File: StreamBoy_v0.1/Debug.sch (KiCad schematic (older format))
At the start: 7 parts

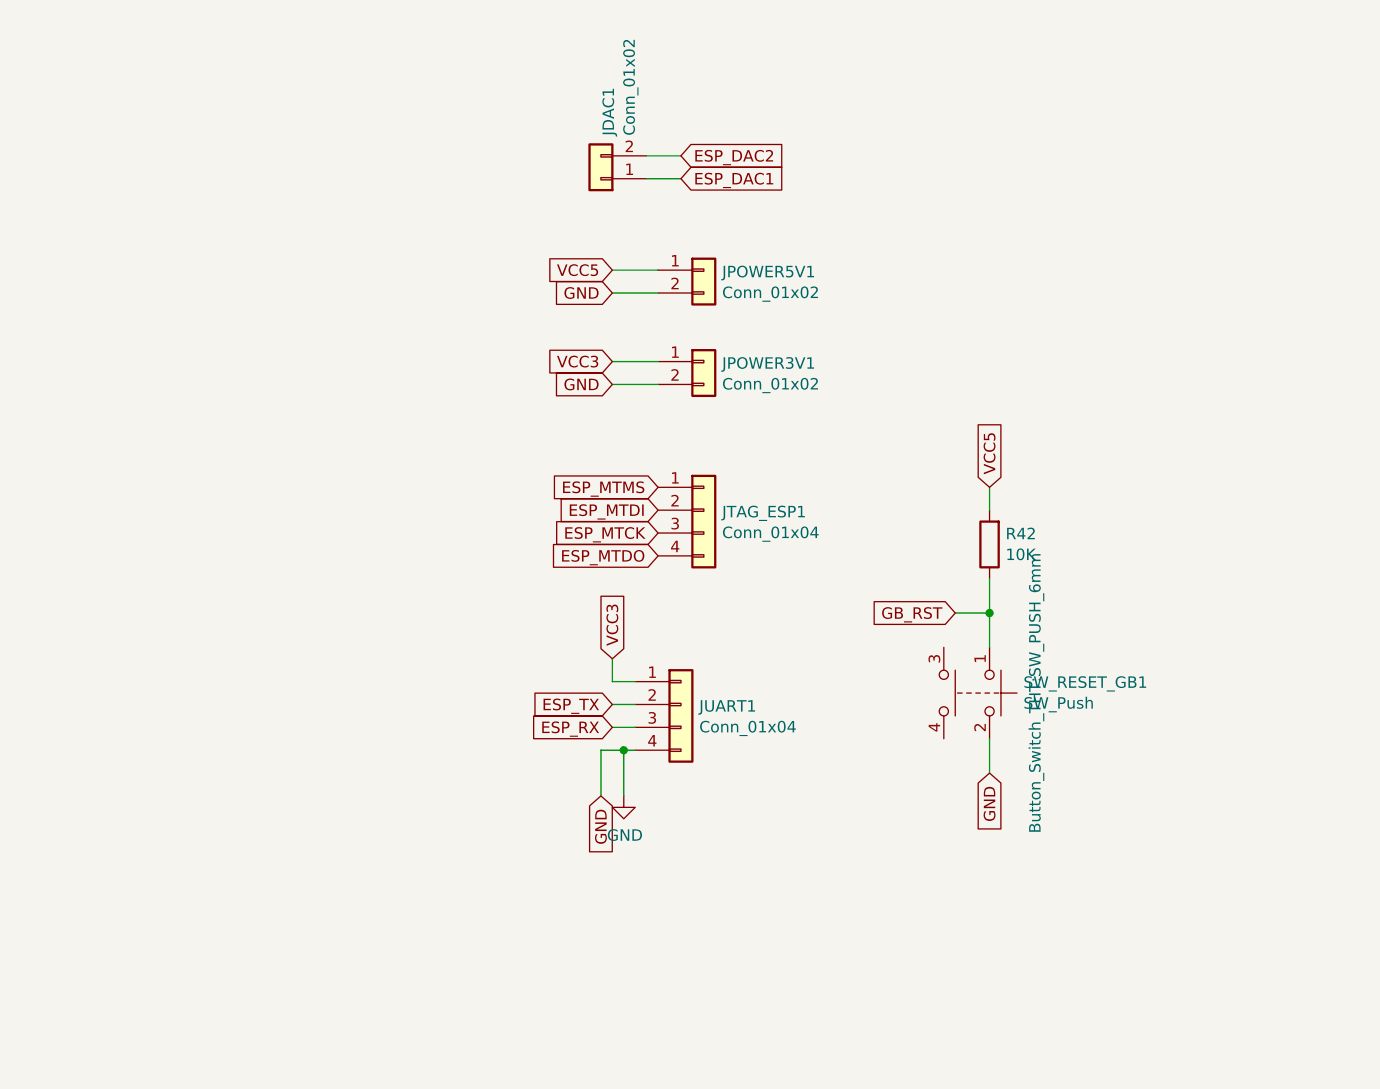
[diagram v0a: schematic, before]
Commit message: Add more debug pins
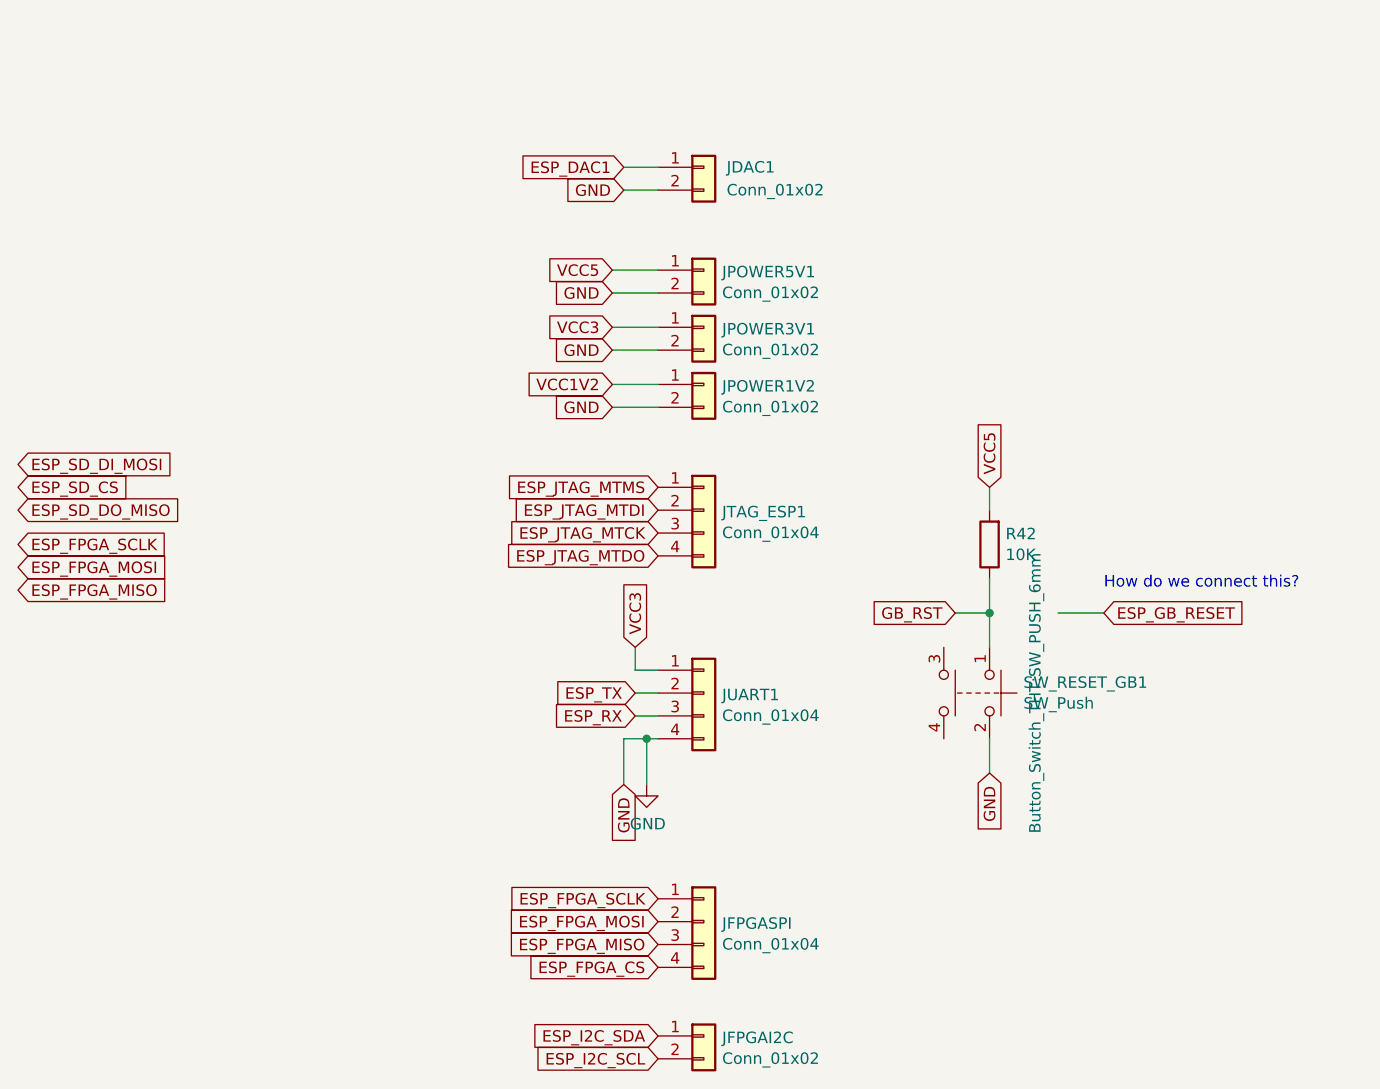
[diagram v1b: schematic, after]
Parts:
- added JFPGAI2C, JPOWER1V2: Conn_01x02, Connector_PinHeader_2.54mm:PinHeader_1x02_P2.54mm_Vertical, symbol Connector_Generic:Conn_01x02
- added JFPGASPI: Conn_01x04, Connector_PinHeader_2.54mm:PinHeader_1x04_P2.54mm_Vertical, symbol Connector_Generic:Conn_01x04
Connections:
- net labels added: ESP_FPGA_CS, ESP_FPGA_MISO, ESP_FPGA_MOSI, ESP_FPGA_SCLK, ESP_GB_RESET, ESP_I2C_SCL, ESP_I2C_SDA, ESP_JTAG_MTCK, ESP_JTAG_MTDI, ESP_JTAG_MTDO, ESP_JTAG_MTMS, ESP_SD_CS, ESP_SD_DI_MOSI, ESP_SD_DO_MISO, VCC1V2
- net labels removed: ESP_DAC2, ESP_MTCK, ESP_MTDI, ESP_MTDO, ESP_MTMS
- wire segments 19 -> 22
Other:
- note added: "How do we connect this?"
- moved on the sheet: JDAC1, JPOWER3V1, JUART1
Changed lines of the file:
@@
 EESchema Schematic File Version 4
-EELAYER 30 0
+LIBS:StreamBoy-cache
+EELAYER 29 0
 EELAYER END
 $Descr A4 11693 8268
@@
 L Connector_Generic:Conn_01x02 JPOWER3V?
 U 1 1 5E0943CE
-P 7500 2350
+P 7500 2200
 AR Path="/5E0943CE" Ref="JPOWER3V?"  Part="1"
 AR Path="/5E087685/5E0943CE" Ref="JPOWER3V1"  Part="1"
-F 0 "JPOWER3V1" H 7580 2342 50  0000 L CNN
-F 1 "Conn_01x02" H 7580 2251 50  0000 L CNN
-F 2 "Connector_PinHeader_2.54mm:PinHeader_1x02_P2.54mm_Vertical" H 7500 2350 50  0001 C CNN
-F 3 "~" H 7500 2350 50  0001 C CNN
-	1    7500 2350
+F 0 "JPOWER3V1" H 7580 2192 50  0000 L CNN
+F 1 "Conn_01x02" H 7580 2101 50  0000 L CNN
+F 2 "Connector_PinHeader_2.54mm:PinHeader_1x02_P2.54mm_Vertical" H 7500 2200 50  0001 C CNN
+F 3 "~" H 7500 2200 50  0001 C CNN
+	1    7500 2200
 	1    0    0    -1
 $EndComp
 Text GLabel 7100 1950 0    50   Input ~ 0
 VCC5
-Text GLabel 7100 2350 0    50   Input ~ 0
+Text GLabel 7100 2200 0    50   Input ~ 0
 VCC3
 Text GLabel 7100 2050 0    50   Input ~ 0
 GND
-Text GLabel 7100 2450 0    50   Input ~ 0
+Text GLabel 7100 2300 0    50   Input ~ 0
 GND
 Wire Wire Line
@@
 	7100 2050 7300 2050
 Wire Wire Line
-	7300 2350 7100 2350
-Wire Wire Line
-	7100 2450 7300 2450
+	7300 2200 7100 2200
+Wire Wire Line
+	7100 2300 7300 2300
 $Comp
 L Connector_Generic:Conn_01x04 JUART?
 U 1 1 5E0943DC
-P 7400 3850
+P 7500 3800
 AR Path="/5E0943DC" Ref="JUART?"  Part="1"
 AR Path="/5E087685/5E0943DC" Ref="JUART1"  Part="1"
-F 0 "JUART1" H 7480 3842 50  0000 L CNN
-F 1 "Conn_01x04" H 7480 3751 50  0000 L CNN
-F 2 "Connector_PinHeader_2.54mm:PinHeader_1x04_P2.54mm_Vertical" H 7400 3850 50  0001 C CNN
-F 3 "~" H 7400 3850 50  0001 C CNN
-	1    7400 3850
-	1    0    0    -1
-$EndComp
-Text GLabel 7100 3650 1    50   Input ~ 0
+F 0 "JUART1" H 7580 3792 50  0000 L CNN
+F 1 "Conn_01x04" H 7580 3701 50  0000 L CNN
+F 2 "Connector_PinHeader_2.54mm:PinHeader_1x04_P2.54mm_Vertical" H 7500 3800 50  0001 C CNN
+F 3 "~" H 7500 3800 50  0001 C CNN
+	1    7500 3800
+	1    0    0    -1
+$EndComp
+Text GLabel 7200 3600 1    50   Input ~ 0
 VCC3
-Text GLabel 7050 4250 3    50   Input ~ 0
+Text GLabel 7150 4200 3    50   Input ~ 0
 GND
 $Comp
 L power:GND #PWR?
 U 1 1 5E0943E4
-P 7150 4250
+P 7250 4200
 AR Path="/5E0943E4" Ref="#PWR?"  Part="1"
 AR Path="/5E087685/5E0943E4" Ref="#PWR0104"  Part="1"
-F 0 "#PWR0104" H 7150 4000 50  0001 C CNN
-F 1 "GND" H 7155 4077 50  0000 C CNN
-F 2 "" H 7150 4250 50  0001 C CNN
-F 3 "" H 7150 4250 50  0001 C CNN
-	1    7150 4250
+F 0 "#PWR0104" H 7250 3950 50  0001 C CNN
+F 1 "GND" H 7255 4027 50  0000 C CNN
+F 2 "" H 7250 4200 50  0001 C CNN
+F 3 "" H 7250 4200 50  0001 C CNN
+	1    7250 4200
 	1    0    0    -1
 $EndComp
@@
 	1    0    0    -1
 $EndComp
-Text GLabel 7300 2900 0    50   Input ~ 0
-ESP_MTMS
-Text GLabel 7300 3000 0    50   Input ~ 0
-ESP_MTDI
-Text GLabel 7300 3100 0    50   Input ~ 0
-ESP_MTCK
-Text GLabel 7300 3200 0    50   Input ~ 0
-ESP_MTDO
-Text GLabel 7100 3950 0    50   Input ~ 0
+Text GLabel 7200 3900 0    50   Input ~ 0
 ESP_RX
-Text GLabel 7100 3850 0    50   Input ~ 0
+Text GLabel 7200 3800 0    50   Input ~ 0
 ESP_TX
 Wire Wire Line
-	7200 3950 7100 3950
-Wire Wire Line
-	7100 3850 7200 3850
-Wire Wire Line
-	7200 4050 7150 4050
-Wire Wire Line
-	7050 4050 7050 4250
-Wire Wire Line
-	7150 4250 7150 4050
-Connection ~ 7150 4050
-Wire Wire Line
-	7150 4050 7050 4050
-Wire Wire Line
-	7200 3750 7100 3750
-Wire Wire Line
-	7100 3750 7100 3650
+	7300 3900 7200 3900
+Wire Wire Line
+	7200 3800 7300 3800
+Wire Wire Line
+	7300 4000 7250 4000
+Wire Wire Line
+	7150 4000 7150 4200
+Wire Wire Line
+	7250 4200 7250 4000
+Connection ~ 7250 4000
+Wire Wire Line
+	7250 4000 7150 4000
+Wire Wire Line
+	7300 3700 7200 3700
+Wire Wire Line
+	7200 3700 7200 3600
 $Comp
 L Device:R R?
@@
 L Connector_Generic:Conn_01x02 JDAC?
 U 1 1 5E094414
-P 7050 1550
+P 7500 1500
 AR Path="/5E094414" Ref="JDAC?"  Part="1"
 AR Path="/5E087685/5E094414" Ref="JDAC1"  Part="1"
-F 0 "JDAC1" V 7016 1362 50  0000 R CNN
-F 1 "Conn_01x02" V 6925 1362 50  0000 R CNN
-F 2 "Connector_PinHeader_2.54mm:PinHeader_1x02_P2.54mm_Vertical" H 7050 1550 50  0001 C CNN
-F 3 "~" H 7050 1550 50  0001 C CNN
-	1    7050 1550
-	-1   0    0    1
-$EndComp
-Text GLabel 7400 1550 2    50   Input ~ 0
+F 0 "JDAC1" H 7600 1500 50  0000 L CNN
+F 1 "Conn_01x02" H 7600 1400 50  0000 L CNN
+F 2 "Connector_PinHeader_2.54mm:PinHeader_1x02_P2.54mm_Vertical" H 7500 1500 50  0001 C CNN
+F 3 "~" H 7500 1500 50  0001 C CNN
+	1    7500 1500
+	1    0    0    -1
+$EndComp
+Text GLabel 7150 1500 0    50   Input ~ 0
 ESP_DAC1
-Text GLabel 7400 1450 2    50   Input ~ 0
-ESP_DAC2
-Wire Wire Line
-	7400 1450 7250 1450
-Wire Wire Line
-	7250 1550 7400 1550
+Wire Wire Line
+	7150 1600 7300 1600
+Wire Wire Line
+	7300 1500 7150 1500
+Text GLabel 9250 3450 2    50   Input ~ 0
+ESP_GB_RESET
+Text GLabel 7300 2900 0    50   Input ~ 0
+ESP_JTAG_MTMS
+Text GLabel 7300 3000 0    50   Input ~ 0
+ESP_JTAG_MTDI
+Text GLabel 7300 3100 0    50   Input ~ 0
+ESP_JTAG_MTCK
+Text GLabel 7300 3200 0    50   Input ~ 0
+ESP_JTAG_MTDO
+Text GLabel 7300 5300 0    50   Input ~ 0
+ESP_I2C_SDA
+Text GLabel 7300 5400 0    50   Input ~ 0
+ESP_I2C_SCL
+Text GLabel 4500 2900 2    50   Input ~ 0
+ESP_SD_CS
+Text GLabel 4500 2800 2    50   Input ~ 0
+ESP_SD_DI_MOSI
+Text GLabel 4500 3000 2    50   Input ~ 0
+ESP_SD_DO_MISO
+Text GLabel 7300 4700 0    50   Input ~ 0
+ESP_FPGA_SCLK
+Text GLabel 7300 4800 0    50   Input ~ 0
+ESP_FPGA_MOSI
+Text GLabel 7300 4900 0    50   Input ~ 0
+ESP_FPGA_MISO
+Text GLabel 4500 3150 2    50   Input ~ 0
+ESP_FPGA_SCLK
+Text GLabel 4500 3250 2    50   Input ~ 0
+ESP_FPGA_MOSI
+Text GLabel 4500 3350 2    50   Input ~ 0
+ESP_FPGA_MISO
+Text GLabel 7300 5000 0    50   Input ~ 0
+ESP_FPGA_CS
+Text Notes 9250 3350 0    50   ~ 0
+How do we connect this?
+$Comp
+L Connector_Generic:Conn_01x04 JTAG_ESP?
+U 1 1 5E164B68
+P 7500 4800
+AR Path="/5E164B68" Ref="JTAG_ESP?"  Part="1"
+AR Path="/5E087685/5E164B68" Ref="JFPGASPI"  Part="1"
+F 0 "JFPGASPI" H 7580 4792 50  0000 L CNN
+F 1 "Conn_01x04" H 7580 4701 50  0000 L CNN
+F 2 "Connector_PinHeader_2.54mm:PinHeader_1x04_P2.54mm_Vertical" H 7500 4800 50  0001 C CNN
+F 3 "~" H 7500 4800 50  0001 C CNN
+	1    7500 4800
+	1    0    0    -1
+$EndComp
+$Comp
+L Connector_Generic:Conn_01x02 JFPGA?
+U 1 1 5E165AC9
+P 7500 5300
+AR Path="/5E165AC9" Ref="JFPGA?"  Part="1"
+AR Path="/5E087685/5E165AC9" Ref="JFPGAI2C"  Part="1"
+F 0 "JFPGAI2C" H 7580 5292 50  0000 L CNN
+F 1 "Conn_01x02" H 7580 5201 50  0000 L CNN
+F 2 "Connector_PinHeader_2.54mm:PinHeader_1x02_P2.54mm_Vertical" H 7500 5300 50  0001 C CNN
+F 3 "~" H 7500 5300 50  0001 C CNN
+	1    7500 5300
+	1    0    0    -1
+$EndComp
+$Comp
+L Connector_Generic:Conn_01x02 JPOWER3V?
+U 1 1 5E166D37
+P 7500 2450
+AR Path="/5E166D37" Ref="JPOWER3V?"  Part="1"
+AR Path="/5E087685/5E166D37" Ref="JPOWER1V2"  Part="1"
+F 0 "JPOWER1V2" H 7580 2442 50  0000 L CNN
+F 1 "Conn_01x02" H 7580 2351 50  0000 L CNN
+F 2 "Connector_PinHeader_2.54mm:PinHeader_1x02_P2.54mm_Vertical" H 7500 2450 50  0001 C CNN
+F 3 "~" H 7500 2450 50  0001 C CNN
+	1    7500 2450
+	1    0    0    -1
+$EndComp
+Text GLabel 7100 2450 0    50   Input ~ 0
+VCC1V2
+Text GLabel 7100 2550 0    50   Input ~ 0
+GND
+Wire Wire Line
+	7300 2450 7100 2450
+Wire Wire Line
+	7100 2550 7300 2550
+Text GLabel 7150 1600 0    50   Input ~ 0
+GND
+Wire Wire Line
+	9250 3450 9050 3450
 $EndSCHEMATC

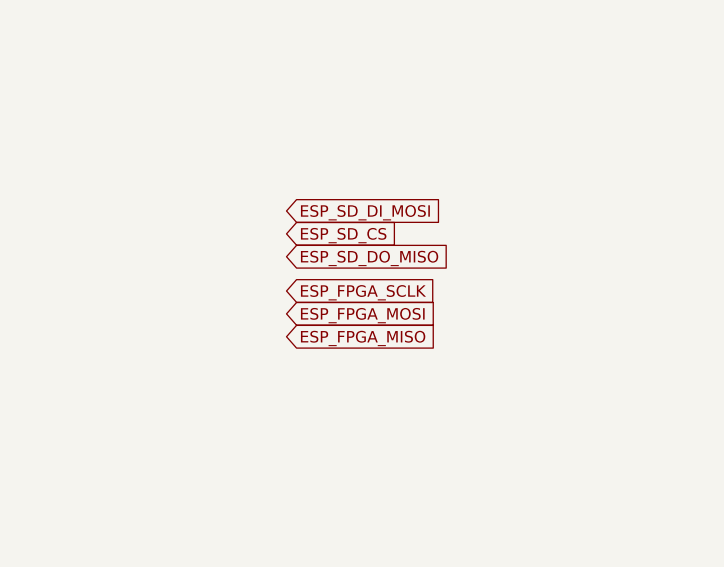
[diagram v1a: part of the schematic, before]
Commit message: Add SD Card to debug
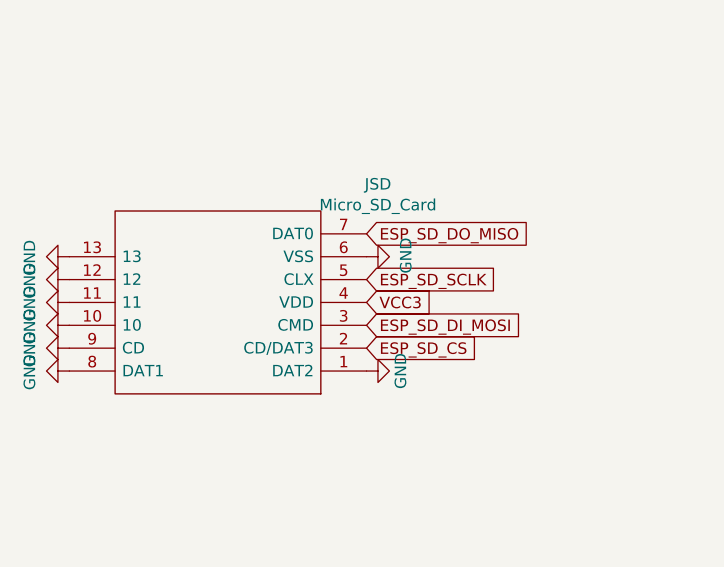
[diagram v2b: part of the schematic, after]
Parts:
- added JSD: Micro_SD_Card, TF-015:TF015, symbol TF-015:TF-015
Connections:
- net labels added: ESP_SD_SCLK
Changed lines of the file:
@@
 Text GLabel 7300 5400 0    50   Input ~ 0
 ESP_I2C_SCL
-Text GLabel 4500 2900 2    50   Input ~ 0
+Text GLabel 4850 3400 2    50   Input ~ 0
 ESP_SD_CS
-Text GLabel 4500 2800 2    50   Input ~ 0
+Text GLabel 4850 3300 2    50   Input ~ 0
 ESP_SD_DI_MOSI
-Text GLabel 4500 3000 2    50   Input ~ 0
+Text GLabel 4850 2900 2    50   Input ~ 0
 ESP_SD_DO_MISO
 Text GLabel 7300 4700 0    50   Input ~ 0
@@
 ESP_FPGA_MOSI
 Text GLabel 7300 4900 0    50   Input ~ 0
-ESP_FPGA_MISO
-Text GLabel 4500 3150 2    50   Input ~ 0
-ESP_FPGA_SCLK
-Text GLabel 4500 3250 2    50   Input ~ 0
-ESP_FPGA_MOSI
-Text GLabel 4500 3350 2    50   Input ~ 0
 ESP_FPGA_MISO
 Text GLabel 7300 5000 0    50   Input ~ 0
@@
 Wire Wire Line
 	9250 3450 9050 3450
+$Comp
+L TF-015:TF-015 JSD
+U 1 1 5E16DC93
+P 4850 3500
+F 0 "JSD" H 4800 2683 50  0000 C CNN
+F 1 "Micro_SD_Card" H 4800 2774 50  0000 C CNN
+F 2 "TF-015:TF015" H 6000 3800 50  0001 C CNN
+F 3 "http://katalog.we-online.de/em/datasheet/693072010801.pdf" H 4850 3500 50  0001 C CNN
+	1    4850 3500
+	-1   0    0    1
+$EndComp
+Text GLabel 4850 3200 2    50   Input ~ 0
+VCC3
+Text GLabel 4850 3100 2    50   Input ~ 0
+ESP_SD_SCLK
+$Comp
+L power:GND #PWR?
+U 1 1 5E17163C
+P 3550 3000
+AR Path="/5E17163C" Ref="#PWR?"  Part="1"
+AR Path="/5E087685/5E17163C" Ref="#PWR?"  Part="1"
+F 0 "#PWR?" H 3550 2750 50  0001 C CNN
+F 1 "GND" H 3555 2827 50  0000 C CNN
+F 2 "" H 3550 3000 50  0001 C CNN
+F 3 "" H 3550 3000 50  0001 C CNN
+	1    3550 3000
+	0    1    1    0
+$EndComp
+$Comp
+L power:GND #PWR?
+U 1 1 5E173646
+P 4850 3000
+AR Path="/5E173646" Ref="#PWR?"  Part="1"
+AR Path="/5E087685/5E173646" Ref="#PWR?"  Part="1"
+F 0 "#PWR?" H 4850 2750 50  0001 C CNN
+F 1 "GND" H 4855 2827 50  0000 C CNN
+F 2 "" H 4850 3000 50  0001 C CNN
+F 3 "" H 4850 3000 50  0001 C CNN
+	1    4850 3000
+	0    -1   -1   0
+$EndComp
+$Comp
+L power:GND #PWR?
+U 1 1 5E172C99
+P 4850 3500
+AR Path="/5E172C99" Ref="#PWR?"  Part="1"
+AR Path="/5E087685/5E172C99" Ref="#PWR?"  Part="1"
+F 0 "#PWR?" H 4850 3250 50  0001 C CNN
+F 1 "GND" H 4850 3350 50  0000 C CNN
+F 2 "" H 4850 3500 50  0001 C CNN
+F 3 "" H 4850 3500 50  0001 C CNN
+	1    4850 3500
+	0    -1   -1   0
+$EndComp
+$Comp
+L power:GND #PWR?
+U 1 1 5E173024
+P 3550 3100
+AR Path="/5E173024" Ref="#PWR?"  Part="1"
+AR Path="/5E087685/5E173024" Ref="#PWR?"  Part="1"
+F 0 "#PWR?" H 3550 2850 50  0001 C CNN
+F 1 "GND" H 3555 2927 50  0000 C CNN
+F 2 "" H 3550 3100 50  0001 C CNN
+F 3 "" H 3550 3100 50  0001 C CNN
+	1    3550 3100
+	0    1    1    0
+$EndComp
+$Comp
+L power:GND #PWR?
+U 1 1 5E096F86
+P 3550 3200
+AR Path="/5E096F86" Ref="#PWR?"  Part="1"
+AR Path="/5E087685/5E096F86" Ref="#PWR?"  Part="1"
+F 0 "#PWR?" H 3550 2950 50  0001 C CNN
+F 1 "GND" H 3555 3027 50  0000 C CNN
+F 2 "" H 3550 3200 50  0001 C CNN
+F 3 "" H 3550 3200 50  0001 C CNN
+	1    3550 3200
+	0    1    1    0
+$EndComp
+$Comp
+L power:GND #PWR?
+U 1 1 5E097212
+P 3550 3300
+AR Path="/5E097212" Ref="#PWR?"  Part="1"
+AR Path="/5E087685/5E097212" Ref="#PWR?"  Part="1"
+F 0 "#PWR?" H 3550 3050 50  0001 C CNN
+F 1 "GND" H 3555 3127 50  0000 C CNN
+F 2 "" H 3550 3300 50  0001 C CNN
+F 3 "" H 3550 3300 50  0001 C CNN
+	1    3550 3300
+	0    1    1    0
+$EndComp
+$Comp
+L power:GND #PWR?
+U 1 1 5E097405
+P 3550 3500
+AR Path="/5E097405" Ref="#PWR?"  Part="1"
+AR Path="/5E087685/5E097405" Ref="#PWR?"  Part="1"
+F 0 "#PWR?" H 3550 3250 50  0001 C CNN
+F 1 "GND" H 3555 3327 50  0000 C CNN
+F 2 "" H 3550 3500 50  0001 C CNN
+F 3 "" H 3550 3500 50  0001 C CNN
+	1    3550 3500
+	0    1    1    0
+$EndComp
+$Comp
+L power:GND #PWR?
+U 1 1 5E097DDA
+P 3550 3400
+AR Path="/5E097DDA" Ref="#PWR?"  Part="1"
+AR Path="/5E087685/5E097DDA" Ref="#PWR?"  Part="1"
+F 0 "#PWR?" H 3550 3150 50  0001 C CNN
+F 1 "GND" H 3555 3227 50  0000 C CNN
+F 2 "" H 3550 3400 50  0001 C CNN
+F 3 "" H 3550 3400 50  0001 C CNN
+	1    3550 3400
+	0    1    1    0
+$EndComp
 $EndSCHEMATC
